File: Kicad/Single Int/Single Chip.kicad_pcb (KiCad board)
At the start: 2 copper layers, 51.3 x 38.1 mm, 3 parts

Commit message: Update PCB
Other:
- board text added: "EMM COMPUTERS V20/V30 (8088/8086) 3.3V Copyright (C) 2023 EMM www.homebrew8088.com"
- board text removed: "EMM COMPUTERS V20/V30 (8088/8086) 3.3V Copyright (C) 2022 EMM www.homebrew8088.com"
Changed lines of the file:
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@@
       (effects (font (size 1 1) (thickness 0.15)))
     )
+    (fp_line (start -0.635 -1.27) (end 1.27 -1.27) (layer F.Fab) (width 0.1))
+    (fp_line (start 1.27 -1.27) (end 1.27 3.81) (layer F.Fab) (width 0.1))
+    (fp_line (start 1.27 3.81) (end -1.27 3.81) (layer F.Fab) (width 0.1))
+    (fp_line (start -1.27 3.81) (end -1.27 -0.635) (layer F.Fab) (width 0.1))
+    (fp_line (start -1.27 -0.635) (end -0.635 -1.27) (layer F.Fab) (width 0.1))
+    (fp_line (start -1.33 3.87) (end 1.33 3.87) (layer F.SilkS) (width 0.12))
+    (fp_line (start -1.33 1.27) (end -1.33 3.87) (layer F.SilkS) (width 0.12))
+    (fp_line (start 1.33 1.27) (end 1.33 3.87) (layer F.SilkS) (width 0.12))
+    (fp_line (start -1.33 1.27) (end 1.33 1.27) (layer F.SilkS) (width 0.12))
+    (fp_line (start -1.33 0) (end -1.33 -1.33) (layer F.SilkS) (width 0.12))
+    (fp_line (start -1.33 -1.33) (end 0 -1.33) (layer F.SilkS) (width 0.12))
+    (fp_line (start -1.8 -1.8) (end -1.8 4.35) (layer F.CrtYd) (width 0.05))
+    (fp_line (start -1.8 4.35) (end 1.8 4.35) (layer F.CrtYd) (width 0.05))
+    (fp_line (start 1.8 4.35) (end 1.8 -1.8) (layer F.CrtYd) (width 0.05))
     (fp_line (start 1.8 -1.8) (end -1.8 -1.8) (layer F.CrtYd) (width 0.05))
-    (fp_line (start 1.8 4.35) (end 1.8 -1.8) (layer F.CrtYd) (width 0.05))
-    (fp_line (start -1.8 4.35) (end 1.8 4.35) (layer F.CrtYd) (width 0.05))
-    (fp_line (start -1.8 -1.8) (end -1.8 4.35) (layer F.CrtYd) (width 0.05))
-    (fp_line (start -1.33 -1.33) (end 0 -1.33) (layer F.SilkS) (width 0.12))
-    (fp_line (start -1.33 0) (end -1.33 -1.33) (layer F.SilkS) (width 0.12))
-    (fp_line (start -1.33 1.27) (end 1.33 1.27) (layer F.SilkS) (width 0.12))
-    (fp_line (start 1.33 1.27) (end 1.33 3.87) (layer F.SilkS) (width 0.12))
-    (fp_line (start -1.33 1.27) (end -1.33 3.87) (layer F.SilkS) (width 0.12))
-    (fp_line (start -1.33 3.87) (end 1.33 3.87) (layer F.SilkS) (width 0.12))
-    (fp_line (start -1.27 -0.635) (end -0.635 -1.27) (layer F.Fab) (width 0.1))
-    (fp_line (start -1.27 3.81) (end -1.27 -0.635) (layer F.Fab) (width 0.1))
-    (fp_line (start 1.27 3.81) (end -1.27 3.81) (layer F.Fab) (width 0.1))
-    (fp_line (start 1.27 -1.27) (end 1.27 3.81) (layer F.Fab) (width 0.1))
-    (fp_line (start -0.635 -1.27) (end 1.27 -1.27) (layer F.Fab) (width 0.1))
     (fp_text user " " (at 0 1.27 90) (layer F.Fab) hide
       (effects (font (size 1 1) (thickness 0.15)))
@@
       (effects (font (size 1 1) (thickness 0.15)) (justify mirror))
     )
+    (fp_line (start 0 1.27) (end 3.81 1.27) (layer B.Fab) (width 0.1))
+    (fp_line (start 3.81 1.27) (end 3.81 -49.53) (layer B.Fab) (width 0.1))
+    (fp_line (start 3.81 -49.53) (end -1.27 -49.53) (layer B.Fab) (width 0.1))
+    (fp_line (start -1.27 -49.53) (end -1.27 0) (layer B.Fab) (width 0.1))
+    (fp_line (start -1.27 0) (end 0 1.27) (layer B.Fab) (width 0.1))
+    (fp_line (start -1.33 -49.59) (end 3.87 -49.59) (layer B.SilkS) (width 0.12))
+    (fp_line (start -1.33 -1.27) (end -1.33 -49.59) (layer B.SilkS) (width 0.12))
+    (fp_line (start 3.87 1.33) (end 3.87 -49.59) (layer B.SilkS) (width 0.12))
+    (fp_line (start -1.33 -1.27) (end 1.27 -1.27) (layer B.SilkS) (width 0.12))
+    (fp_line (start 1.27 -1.27) (end 1.27 1.33) (layer B.SilkS) (width 0.12))
+    (fp_line (start 1.27 1.33) (end 3.87 1.33) (layer B.SilkS) (width 0.12))
+    (fp_line (start -1.33 0) (end -1.33 1.33) (layer B.SilkS) (width 0.12))
+    (fp_line (start -1.33 1.33) (end 0 1.33) (layer B.SilkS) (width 0.12))
+    (fp_line (start -1.8 1.8) (end -1.8 -50.05) (layer B.CrtYd) (width 0.05))
+    (fp_line (start -1.8 -50.05) (end 4.35 -50.05) (layer B.CrtYd) (width 0.05))
+    (fp_line (start 4.35 -50.05) (end 4.35 1.8) (layer B.CrtYd) (width 0.05))
     (fp_line (start 4.35 1.8) (end -1.8 1.8) (layer B.CrtYd) (width 0.05))
-    (fp_line (start 4.35 -50.05) (end 4.35 1.8) (layer B.CrtYd) (width 0.05))
-    (fp_line (start -1.8 -50.05) (end 4.35 -50.05) (layer B.CrtYd) (width 0.05))
-    (fp_line (start -1.8 1.8) (end -1.8 -50.05) (layer B.CrtYd) (width 0.05))
-    (fp_line (start -1.33 1.33) (end 0 1.33) (layer B.SilkS) (width 0.12))
-    (fp_line (start -1.33 0) (end -1.33 1.33) (layer B.SilkS) (width 0.12))
-    (fp_line (start 1.27 1.33) (end 3.87 1.33) (layer B.SilkS) (width 0.12))
-    (fp_line (start 1.27 -1.27) (end 1.27 1.33) (layer B.SilkS) (width 0.12))
-    (fp_line (start -1.33 -1.27) (end 1.27 -1.27) (layer B.SilkS) (width 0.12))
-    (fp_line (start 3.87 1.33) (end 3.87 -49.59) (layer B.SilkS) (width 0.12))
-    (fp_line (start -1.33 -1.27) (end -1.33 -49.59) (layer B.SilkS) (width 0.12))
-    (fp_line (start -1.33 -49.59) (end 3.87 -49.59) (layer B.SilkS) (width 0.12))
-    (fp_line (start -1.27 0) (end 0 1.27) (layer B.Fab) (width 0.1))
-    (fp_line (start -1.27 -49.53) (end -1.27 0) (layer B.Fab) (width 0.1))
-    (fp_line (start 3.81 -49.53) (end -1.27 -49.53) (layer B.Fab) (width 0.1))
-    (fp_line (start 3.81 1.27) (end 3.81 -49.53) (layer B.Fab) (width 0.1))
-    (fp_line (start 0 1.27) (end 3.81 1.27) (layer B.Fab) (width 0.1))
     (fp_text user " " (at 1.27 -24.13 180) (layer B.Fab) hide
       (effects (font (size 1 1) (thickness 0.15)) (justify mirror))
@@
       (effects (font (size 1 1) (thickness 0.15)))
     )
+    (fp_line (start 16.3 -1.55) (end -1.05 -1.55) (layer F.CrtYd) (width 0.05))
+    (fp_line (start 16.3 49.8) (end 16.3 -1.55) (layer F.CrtYd) (width 0.05))
+    (fp_line (start -1.05 49.8) (end 16.3 49.8) (layer F.CrtYd) (width 0.05))
+    (fp_line (start -1.05 -1.55) (end -1.05 49.8) (layer F.CrtYd) (width 0.05))
+    (fp_line (start 14.08 -1.33) (end 8.62 -1.33) (layer F.SilkS) (width 0.12))
+    (fp_line (start 14.08 49.59) (end 14.08 -1.33) (layer F.SilkS) (width 0.12))
+    (fp_line (start 1.16 49.59) (end 14.08 49.59) (layer F.SilkS) (width 0.12))
+    (fp_line (start 1.16 -1.33) (end 1.16 49.59) (layer F.SilkS) (width 0.12))
+    (fp_line (start 6.62 -1.33) (end 1.16 -1.33) (layer F.SilkS) (width 0.12))
+    (fp_line (start 0.255 -0.27) (end 1.255 -1.27) (layer F.Fab) (width 0.1))
+    (fp_line (start 0.255 49.53) (end 0.255 -0.27) (layer F.Fab) (width 0.1))
+    (fp_line (start 14.985 49.53) (end 0.255 49.53) (layer F.Fab) (width 0.1))
+    (fp_line (start 14.985 -1.27) (end 14.985 49.53) (layer F.Fab) (width 0.1))
     (fp_line (start 1.255 -1.27) (end 14.985 -1.27) (layer F.Fab) (width 0.1))
-    (fp_line (start 14.985 -1.27) (end 14.985 49.53) (layer F.Fab) (width 0.1))
-    (fp_line (start 14.985 49.53) (end 0.255 49.53) (layer F.Fab) (width 0.1))
-    (fp_line (start 0.255 49.53) (end 0.255 -0.27) (layer F.Fab) (width 0.1))
-    (fp_line (start 0.255 -0.27) (end 1.255 -1.27) (layer F.Fab) (width 0.1))
-    (fp_line (start 6.62 -1.33) (end 1.16 -1.33) (layer F.SilkS) (width 0.12))
-    (fp_line (start 1.16 -1.33) (end 1.16 49.59) (layer F.SilkS) (width 0.12))
-    (fp_line (start 1.16 49.59) (end 14.08 49.59) (layer F.SilkS) (width 0.12))
-    (fp_line (start 14.08 49.59) (end 14.08 -1.33) (layer F.SilkS) (width 0.12))
-    (fp_line (start 14.08 -1.33) (end 8.62 -1.33) (layer F.SilkS) (width 0.12))
-    (fp_line (start -1.05 -1.55) (end -1.05 49.8) (layer F.CrtYd) (width 0.05))
-    (fp_line (start -1.05 49.8) (end 16.3 49.8) (layer F.CrtYd) (width 0.05))
-    (fp_line (start 16.3 49.8) (end 16.3 -1.55) (layer F.CrtYd) (width 0.05))
-    (fp_line (start 16.3 -1.55) (end -1.05 -1.55) (layer F.CrtYd) (width 0.05))
     (fp_arc (start 7.62 -1.33) (end 6.62 -1.33) (angle -180) (layer F.SilkS) (width 0.12))
     (fp_text user " " (at 7.62 24.13 90) (layer F.Fab) hide
@@
     (effects (font (size 0.762 0.762) (thickness 0.15)) (justify left))
   )
-  (gr_text "EMM COMPUTERS\nV20/V30 (8088/8086) 3.3V \nCopyright (C) 2022 EMM\nwww.homebrew8088.com" (at 139.7 86.614) (layer F.SilkS)
+  (gr_text "EMM COMPUTERS\nV20/V30 (8088/8086) 3.3V \nCopyright (C) 2023 EMM\nwww.homebrew8088.com" (at 139.7 86.614) (layer F.SilkS)
     (effects (font (size 1 1) (thickness 0.15)) (justify left))
   )

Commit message: Fixed Schematic and PCB
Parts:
- removed  : , Connector_PinHeader_2.54mm:PinHeader_1x02_P2.54mm_Vertical
- removed ?: , Connector_PinHeader_2.54mm:PinHeader_2x20_P2.54mm_Vertical
- removed ?: , Package_DIP:DIP-40_W15.24mm
- added J1: Raspberry_Pi_2_3, Connector_PinHeader_2.54mm:PinHeader_2x20_P2.54mm_Vertical, B.Cu at (124.5, 95.0)
- added J2: Conn_01x02, Connector_PinHeader_2.54mm:PinHeader_1x02_P2.54mm_Vertical, F.Cu at (128.8, 89.7)
- added U1: 8088_Min_Mode, Socket:DIP_Socket-40_W11.9_W12.7_W15.24_W17.78_W18.5_3M_240-1280-00-0602J, F.Cu at (124.5, 80.3)
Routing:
- net /RD: track 41.1 -> 0.00 mm
- net /DTR: track 0.00 -> 41.1 mm
- net /3.3V: track 81.6 -> 80.6 mm
- net /5+: track 9.63 -> 8.61 mm
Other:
- net class Default removed
- board text added: "APR 23"
- board text removed: "APR 22"

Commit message: Gerber
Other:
- board text added: "MAR 23"
- board text removed: "APR 23"
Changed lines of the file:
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@@
     (effects (font (size 0.762 0.762) (thickness 0.15)) (justify left))
   )
-  (gr_text "APR 23" (at 169.672 100.584) (layer "F.SilkS")
+  (gr_text "MAR 23" (at 169.672 100.584) (layer "F.SilkS")
     (effects (font (size 0.762 0.762) (thickness 0.15)) (justify left))
   )

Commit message: UPDATE
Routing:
- net /5+: track 8.61 -> 7.89 mm
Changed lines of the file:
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@@
   (segment (start 128.27 96.266) (end 127 97.536) (width 0.25) (layer "F.Cu") (net 1))
   (segment (start 128.27 90.17) (end 128.27 96.266) (width 0.25) (layer "F.Cu") (net 1))
-  (segment (start 128.778 89.662) (end 128.27 90.17) (width 0.25) (layer "F.Cu") (net 1))
   (segment (start 147.32 76.073) (end 147.32 65.024) (width 0.25) (layer "F.Cu") (net 2))
   (segment (start 172.72 80.264) (end 172.72 94.996) (width 0.25) (layer "F.Cu") (net 2))
@@
   (segment (start 140.97 86.36) (end 140.97 96.266) (width 0.25) (layer "F.Cu") (net 5))
   (segment (start 140.97 73.533) (end 137.16 69.723) (width 0.25) (layer "F.Cu") (net 6))
-  (segment (start 143.51 86.868) (end 143.51 86.36) (width 0.25) (layer "F.Cu") (net 6))
-  (segment (start 143.51 96.266) (end 143.51 86.614) (width 0.25) (layer "F.Cu") (net 6))
+  (segment (start 143.51 96.266) (end 143.51 86.36) (width 0.25) (layer "F.Cu") (net 6))
   (segment (start 144.78 97.536) (end 143.51 96.266) (width 0.25) (layer "F.Cu") (net 6))
   (segment (start 143.51 86.36) (end 140.97 83.82) (width 0.25) (layer "F.Cu") (net 6))

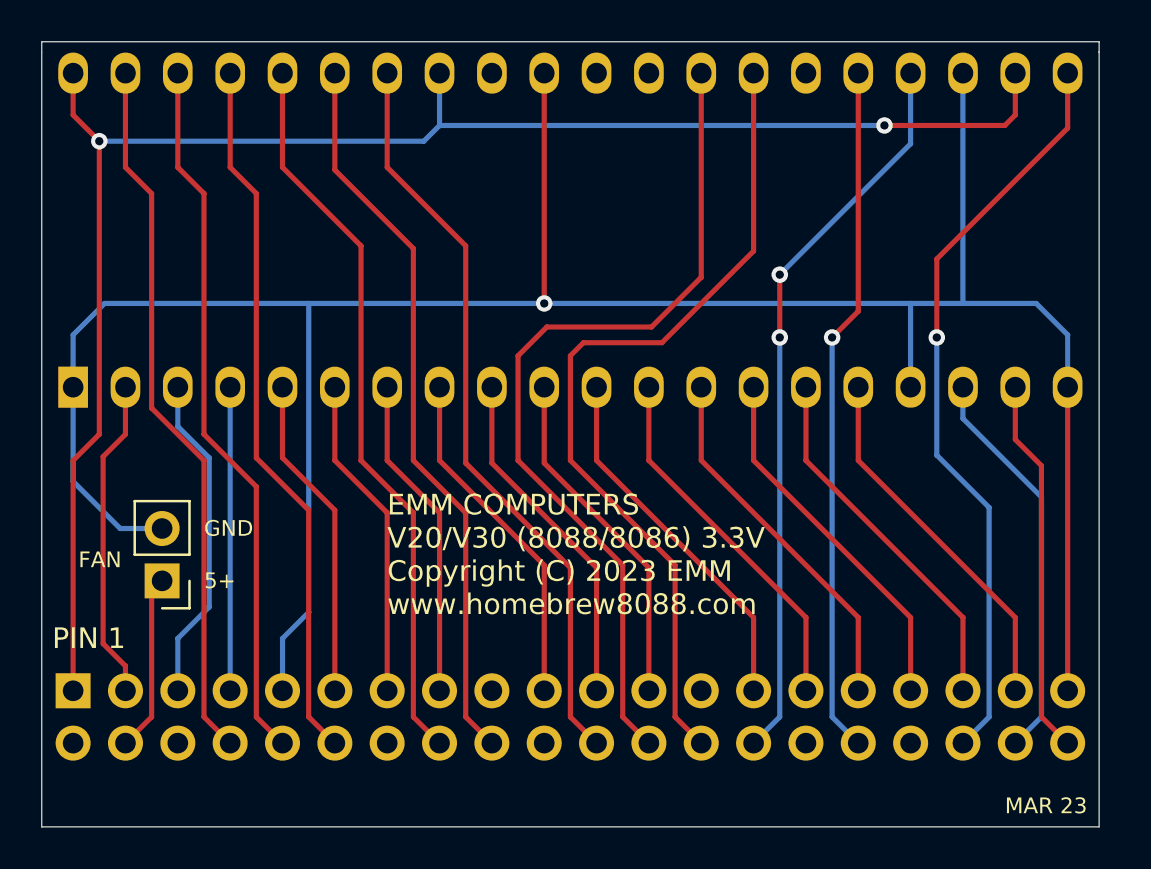
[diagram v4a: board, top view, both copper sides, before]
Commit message: switched back to socket
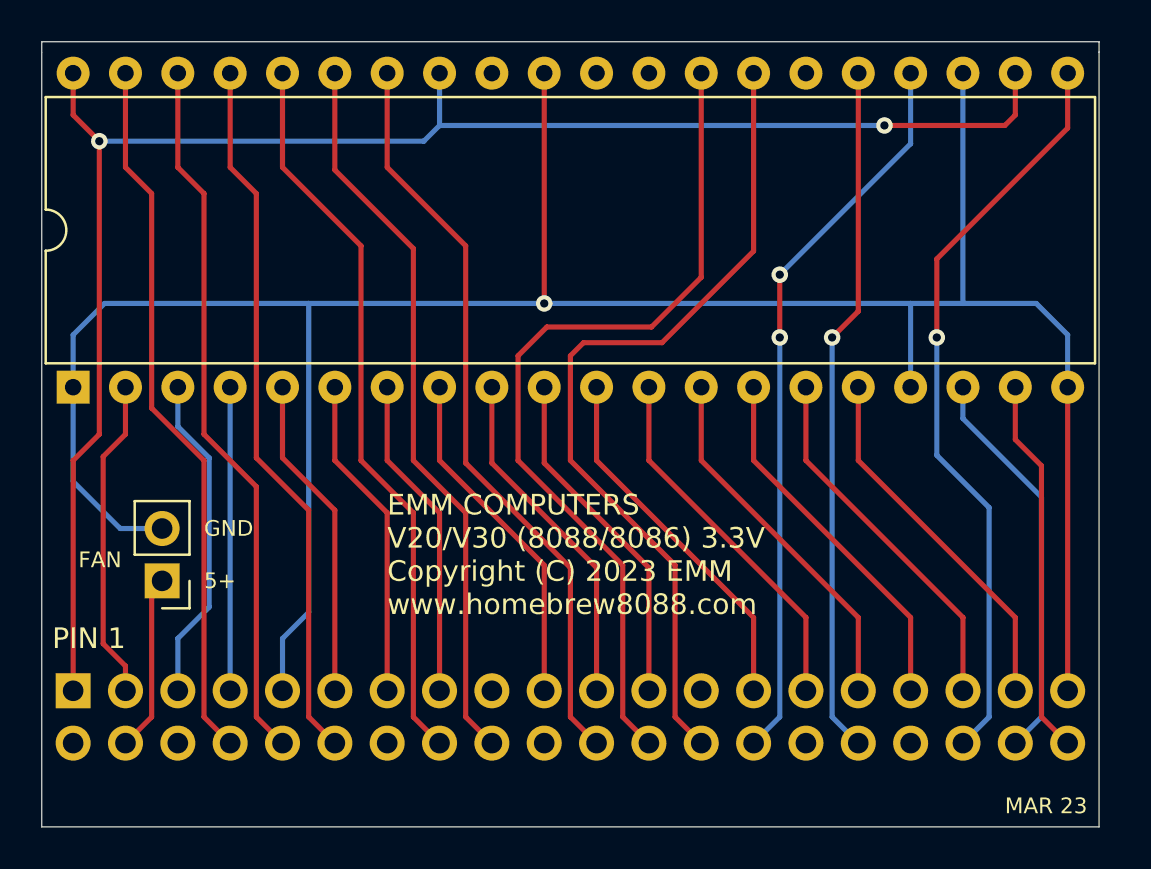
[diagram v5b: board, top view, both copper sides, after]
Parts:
- U1: footprint Socket:DIP_Socket-40_W11.9_W12.7_W15.24_W17.78_W18.5_3M_240-1280-00-0602J -> Package_DIP:DIP-40_W15.24mm
